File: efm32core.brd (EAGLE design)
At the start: 52.1 x 53.3 mm, 45 parts, among them U1 IP4220CZ6SSOT-6, X1 48.0MHz, X2 32.768kHz

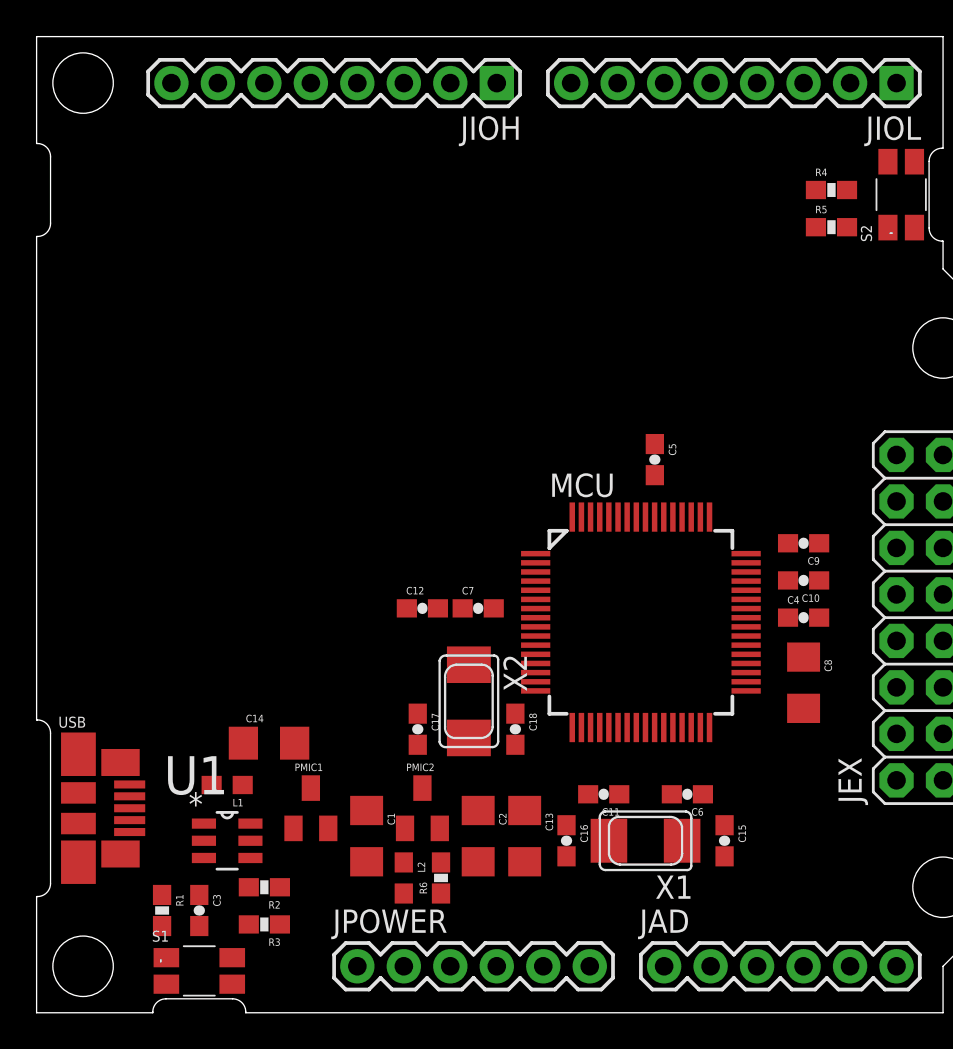
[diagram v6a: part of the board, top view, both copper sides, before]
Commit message: add up bluetooth module and microsd socket
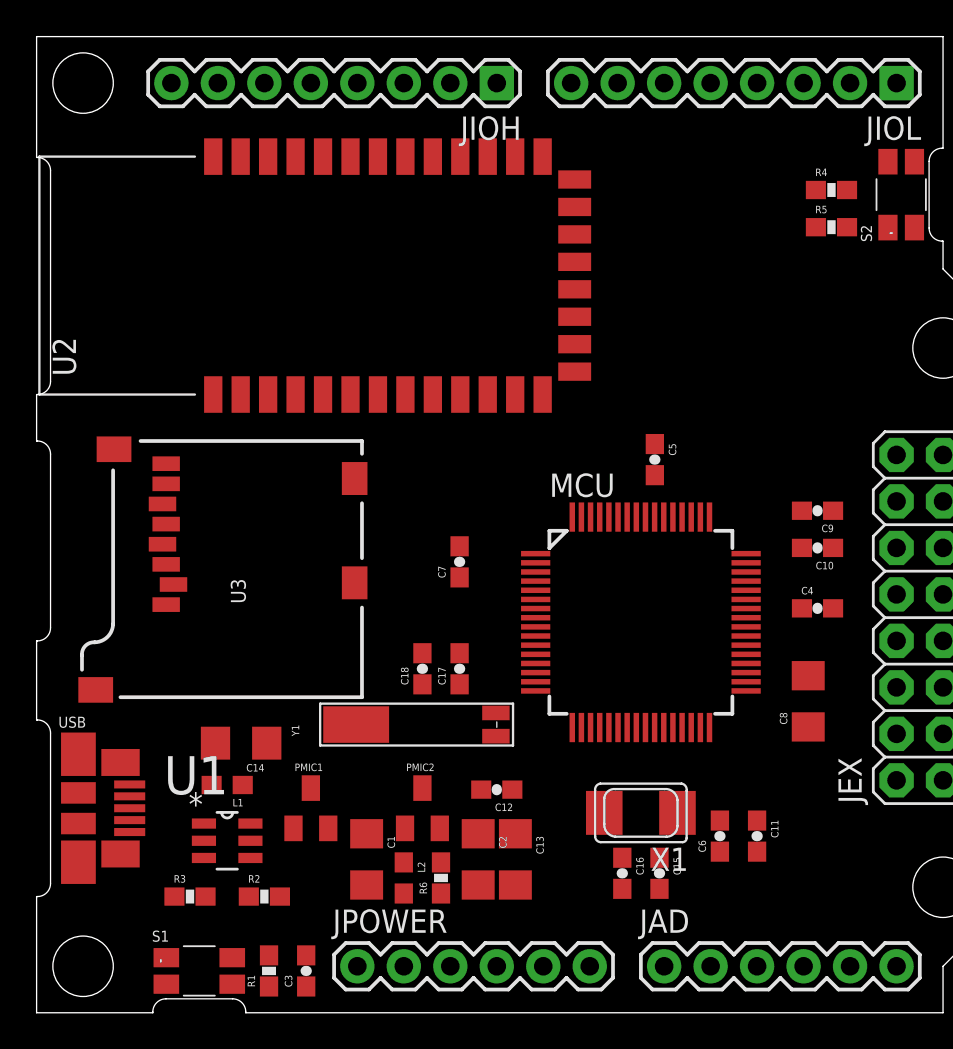
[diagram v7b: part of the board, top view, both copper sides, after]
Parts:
- removed X2: 32.768kHz, adafruit:NX5032
- added U2: HC_05, SerialPortBluetooth:BLUETOOTH_SMD
- added U3: USD-SOCKETNEW, SparkFun-Connectors:MICRO-SD-SOCKET-PP
- added Y1: 32.768kHz, SparkFun-FreqCtrl:CRYSTAL-32KHZ-SMD-MS3V-T1R
- moved GECKO 32.2 mm to (39.3, 37.9), flipped to the top, turned to 90 degrees
- moved C12 10.7 mm to (25.1, 12.2), turned to 180 degrees
- moved C11 8.69 mm to (39.4, 9.65), turned to 270 degrees
- moved R1 6.71 mm to (12.7, 2.29), turned to 90 degrees
- moved C3 6.71 mm to (14.7, 2.29), turned to 90 degrees
- moved C18 6.06 mm to (21.1, 18.8), turned to 90 degrees
- moved R3 4.34 mm to (8.38, 6.35), turned to 0 degrees
- moved C17 4.02 mm to (23.1, 18.8), turned to 90 degrees
- moved C15 3.98 mm to (34.0, 7.62)
- moved C16 3.53 mm to (32.0, 7.62)
- moved C6 2.90 mm to (37.3, 9.65), turned to 90 degrees
- moved C7 2.74 mm to (23.1, 24.6), turned to 90 degrees
- moved C10 1.93 mm to (42.7, 25.4)
- moved C9 1.93 mm to (42.7, 27.4)
- moved X1 1.55 mm to (33.0, 10.9)
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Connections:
- new net LEU1_RX: MCU.38
- new net LEU1_TX: MCU.37
- new net US0_RX: MCU.60
- new net US0_TX: MCU.59
- new net US1_RX: MCU.10, U2.1
- new net US1_TX: MCU.9, U2.2
- new net US2_CLK: MCU.13, U3.5
- new net US2_CS: MCU.14, U3.2
- new net US2_RX: MCU.12, U3.7
- new net US2_TX: MCU.11, U3.3
- net 3.3V: now also U3.4
- net GND: now also U3.6
- net LFXTAL_N: now also Y1.X1; no longer X2.P$1
- net LFXTAL_P: now also Y1.X2; no longer X2.P$2
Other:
- outline, holes or cut-outs redrawn

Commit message: update a bit
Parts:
- added U4: MPU-6000QFN-24, SparkFun-Sensors:QFN-24-TESTING
- moved GECKO 7.23 mm to (37.0, 44.8)
- moved JPOWER 1.02 mm to (16.5, 2.54)
- moved S1 0.76 mm to (8.13, 2.29)
- moved STANDOFF3 0.76 mm to (49.5, 7.62)
- moved STANDOFF4 0.76 mm to (49.5, 35.6)
- moved C3 0.76 mm to (14.0, 2.29)
- moved R1 0.76 mm to (11.9, 2.29)
- moved R4 0.51 mm to (43.4, 45.5)
- moved S2 0.51 mm to (47.2, 45.2)
- moved R5 0.51 mm to (43.4, 43.4)
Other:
- outline, holes or cut-outs redrawn
